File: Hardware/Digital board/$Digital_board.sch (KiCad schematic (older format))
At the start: 255 parts, among them P1 1.8MHz osc, P2 SW_DIP9, P3 CONN_01X04, P4 CONN_02X32, P5 CONN_02X20, P6 CONN_01X03, P7 CONN_02X05, U1 7402, U10 74LS688, U100 74LS373, U101 74LS688, U102 74LS688, U103 74LS688, U104 74LS688, U105 4040, U106 4040, U107 4040, U108 4040, U109 74HCT02, U11 74LS688, U110 74LS688, U111 74LS688, U112 4040, U113 4040, U114 74LS688, U115 74LS688, U116 4040, U117 4040, U118 74LS373, U119 74LS373, U12 4040, U120 74LS373, U121 74LS373, U122 74LS32, U123 4040, U124 4040, U125 74LS541, U126 74LS541, U127 SST39SF020, U128 SST39SF020, U129 74LS30, U13 4040, U130 74LS30, U131 4040, U132 SST39SF020, U133 4040, U134 4040, U135 74LS688, U136 74HCT02, U137 4040, U138 74LS08, U139 4040, U14 4040, U140 74LS688, U141 74LS688, U142 74LS238, U143 74LS373, U144 74LS373, U145 74LS238, U146 74LS373, U147 74LS373, U148 74LS373, U149 4040, U15 4040, U150 74LS688, U151 4040, U152 74LS688, U153 4040, U154 74LS688, U155 74HCT02, U156 4040, U157 4040, U158 74LS688, U159 74LS688, U16 74LS541, U160 4040, U161 74LS373, U162 74LS688, U163 74LS373, U164 74LS373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

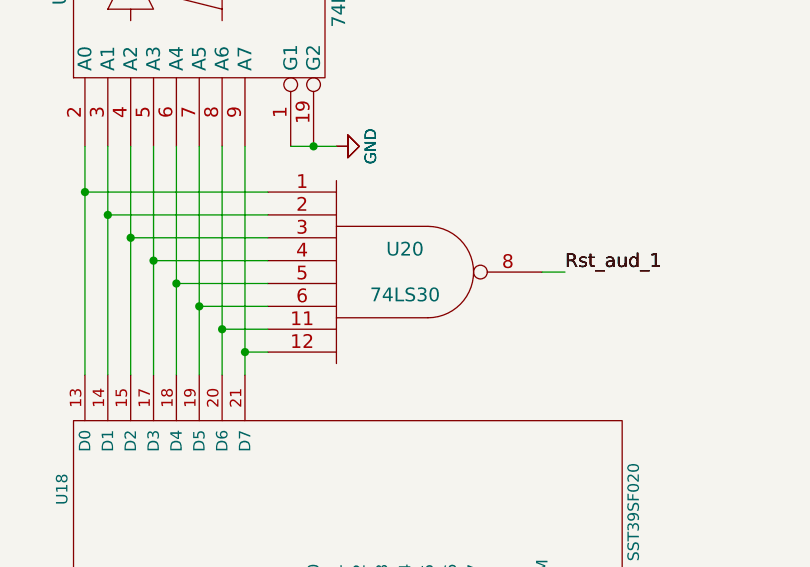
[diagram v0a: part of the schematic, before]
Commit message: Components association
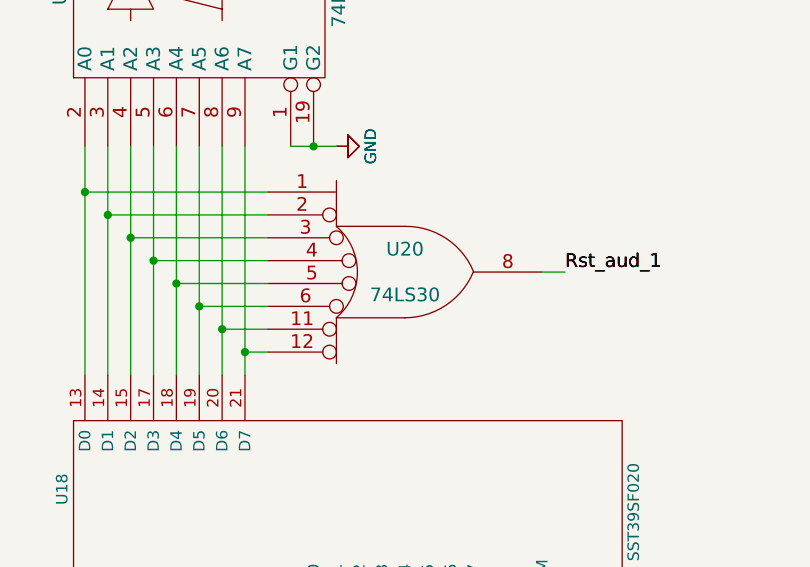
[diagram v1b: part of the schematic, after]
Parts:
- U100, U101, U102, U103, U104, U110, U111, U114, U115, U118, U119, U120, U121, U125, U126, U135, U140, U141, U143, U144, U146, U147, U148, U150, U152, U154, U158, U159, U161, U162, U163, U164, U165, U166, U167, U168, U171, U173, U175, U176, U178, U185, U187, U188, U190, U193, U194, U195, U196, U200, U201, U203, U205, U206, U207, U209, U211, U214, U215, U217, U221, U223, U224, U225, U229, U23, U230, U231, U233, U234, U235, U236, U237, U239, U24, U242, U243, U244, U27, U28, U32, U33, U34, U35, U40, U41, U42, U43, U45, U47, U48, U49, U50, U56, U57, U60, U61, U62, U66, U67, U68, U69, U70, U72, U73, U74, U75, U76, U77, U78, U79, U85, U86, U89, U90, U93, U94, U95, U96, U97, U98, U99: footprint (none) -> Sockets_DIP:DIP-20__300
- U105, U106, U107, U108, U112, U113, U116, U117, U123, U124, U131, U133, U134, U137, U139, U142, U145, U149, U151, U153, U156, U157, U160, U169, U172, U174, U177, U182, U183, U184, U186, U192, U198, U212, U213, U216, U220, U222, U226, U227, U228, U232, U238, U240, U241, U25, U26, U29, U30, U31, U36, U37, U51, U52, U53, U54, U58, U59, U63, U64, U65, U71, U80, U81, U82, U83, U87, U88, U91, U92: footprint (none) -> Sockets_DIP:DIP-16__300
- U109, U129, U130, U136, U138, U155, U170, U179, U180, U181, U189, U191, U197, U199, U20, U202, U204, U208, U21, U210, U218, U219, U22, U38, U39, U44, U46, U55, U84: footprint (none) -> Sockets_DIP:DIP-14__300
- U122: footprint (none) -> Sockets_DIP:DIP-8__300
- U127, U128, U132: footprint (none) -> Sockets_DIP:DIP-32__600
